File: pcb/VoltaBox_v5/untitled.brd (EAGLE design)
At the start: 80 x 60 mm, 63 parts, among them J1 0, X1 112J-TDAR-R(MICROSD), X2 52892-0895, X3 52892-0895, X4 XT30PW-F, X6 XT60PW-M, X7 KLS1-233

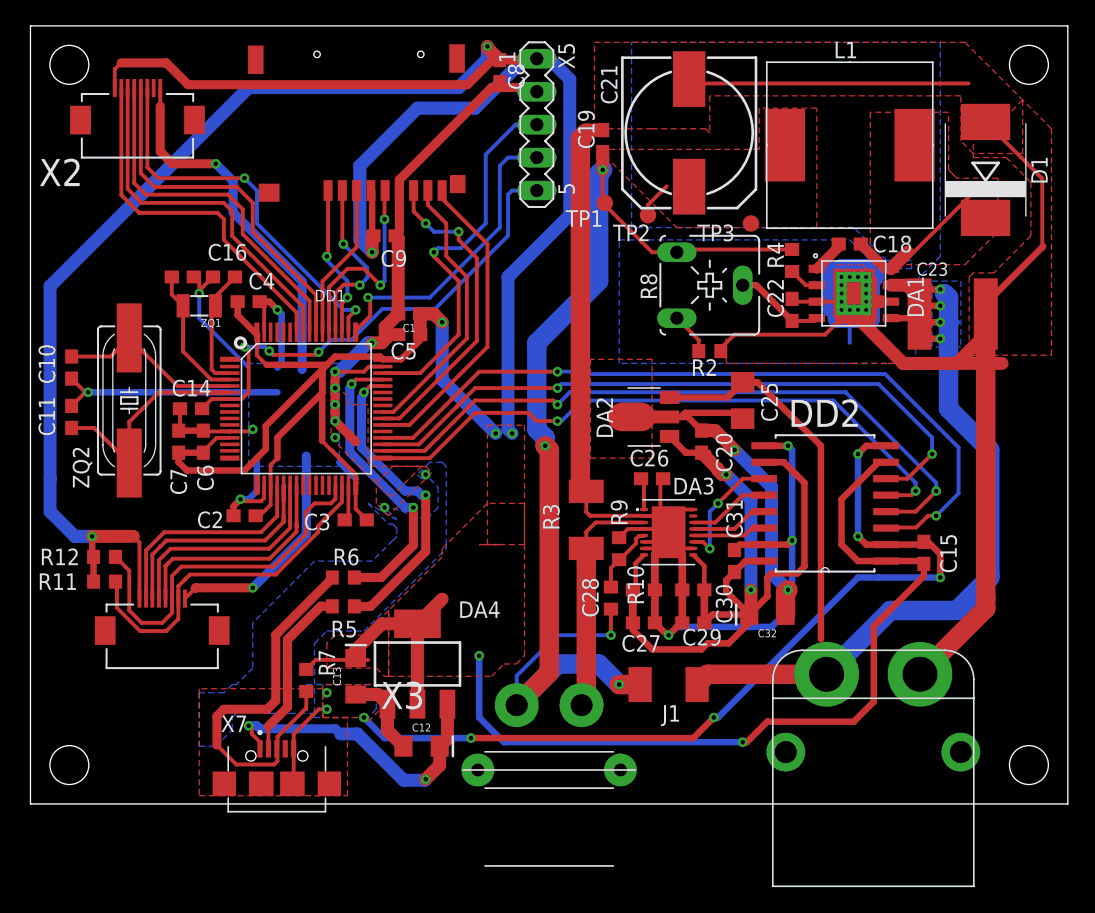
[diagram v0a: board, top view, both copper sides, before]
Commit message: Changed all GND nets in dc-dc and adc part to AGND. Changed usb footprint to correct usb footprint (kls1-233-1-x-x to kls1-233-0-x-x (it's doesn't need holes in pcb that must be very close to the connector's pads)). X2 shifted down. Added some via in dc-dc.
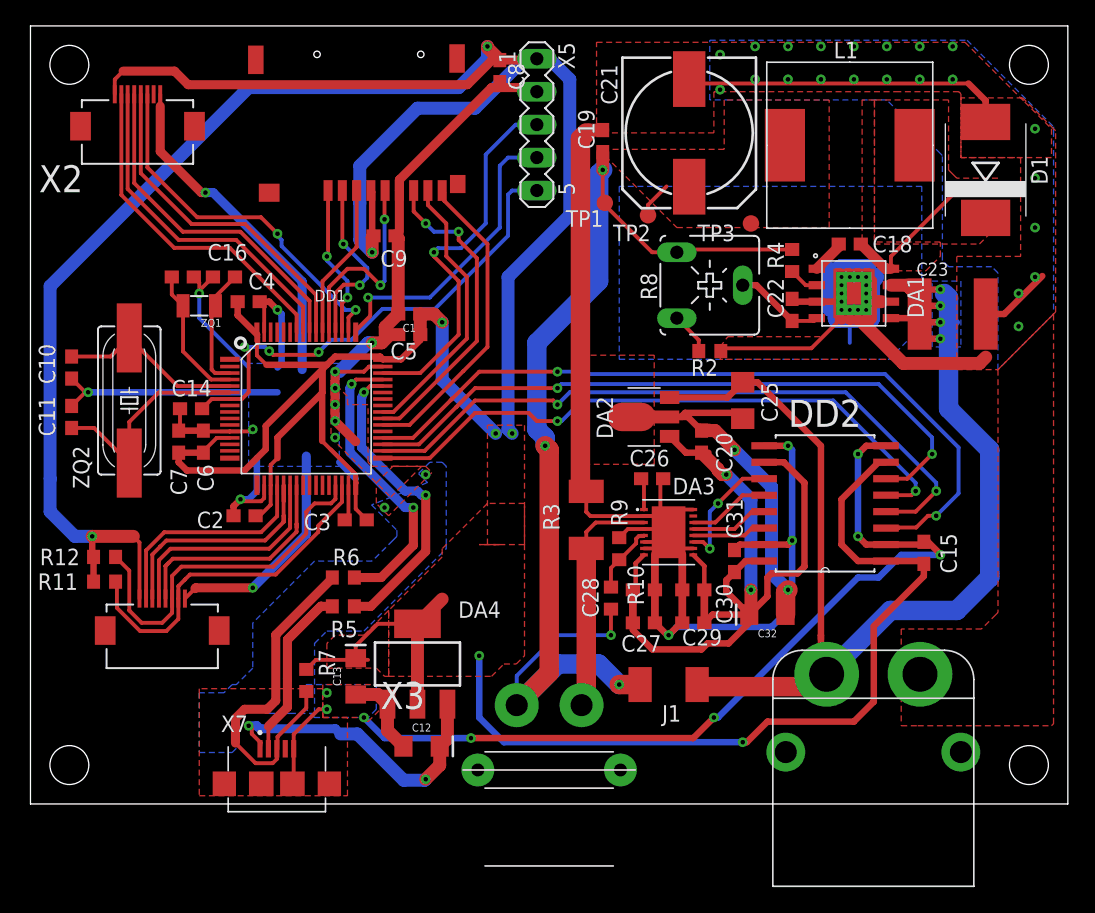
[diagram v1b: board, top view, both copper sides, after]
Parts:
- moved X2 0.48 mm to (8.26, 57.6)
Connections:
- new net AGND: C19.2, C20.2, C21.-, C22.2, C23.2, C25.2, C26.2, C27.2, C28.2, C29.2, C30.2, C31.2, C32.-, D1.A, DA1.3, DA1.6, DA1.P$10, DA1.P$11, DA1.P$12, DA1.P$13, DA1.P$14, DA1.P$15, DA1.P$16, DA1.P$17, DA1.P$18, DA1.P$19, DA1.P$20, DA1.P$21, DA1.P$22, DA1.P$9, DA2.2, DA2.2@1, DA3.10, DA3.16, DA3.17, DA3.2, DA3.4, DA3.6, DA3.7, DD2.15, DD2.9, R2.1, R3.1, R9.1, X6.P$1
- net GND: no longer C19.2, C20.2, C21.-, C22.2, C23.2, C25.2, C26.2, C27.2, C28.2, C29.2, C30.2, C31.2, C32.-, D1.A, DA1.3, DA1.6, DA1.P$10, DA1.P$11, DA1.P$12, DA1.P$13, DA1.P$14, DA1.P$15, DA1.P$16, DA1.P$17, DA1.P$18, DA1.P$19, DA1.P$20, DA1.P$21, DA1.P$22, DA1.P$9, DA2.2, DA2.2@1, DA3.10, DA3.16, DA3.17, DA3.2, DA3.4, DA3.6, DA3.7, DD2.15, DD2.9, R2.1, R3.1, R9.1, X6.P$1
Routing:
- net GND: track 488.2 -> 226.2 mm, vias 28 -> 23
- net AGND: track 0.00 -> 213.2 mm, vias 0 -> 27
- net +12V: track 93.7 -> 97.0 mm
- net D_P: track 30.3 -> 27.0 mm
- net OLED_SCK: track 28.1 -> 26.4 mm
- net OLED_RS: track 28.1 -> 26.6 mm
- net OLED_MOSI: track 28.1 -> 26.6 mm
- net OLED_CS: track 30.2 -> 28.6 mm
- net N$9: track 13.5 -> 11.9 mm
- net OLED_DC: track 28.0 -> 26.5 mm
- added copper zone on layer 1, net AGND
- added copper zone on layer 16, net AGND

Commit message: Relocated all silk labels to it's places. Renamed isolator's model. Added some text to the top silk (tPlace).
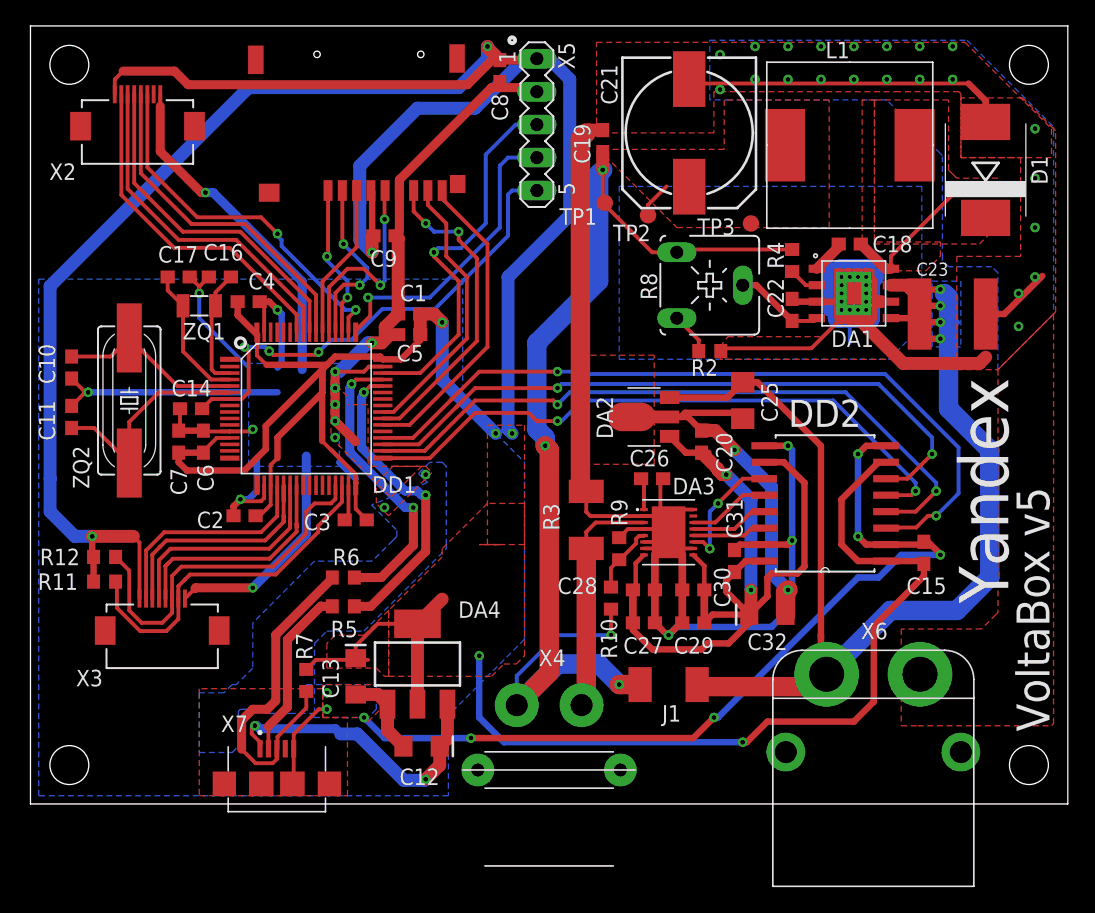
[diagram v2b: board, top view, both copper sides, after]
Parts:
- DD2: value ADUM1401WTRWZ -> ADUM1401CRWZ; device ADUM1401WTRWZ:SOIC127P1032X265-16N -> ADUM1401WTRWZ:SO-16W
- moved C17 0.32 mm to (11.4, 40.6)
- moved C16 0.32 mm to (14.6, 40.6)
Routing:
- net D_P: track 27.0 -> 26.2 mm
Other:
- board text added: "VoltaBox v5"
- board text added: "Yandex"
